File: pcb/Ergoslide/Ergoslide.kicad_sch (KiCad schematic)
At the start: 170 parts

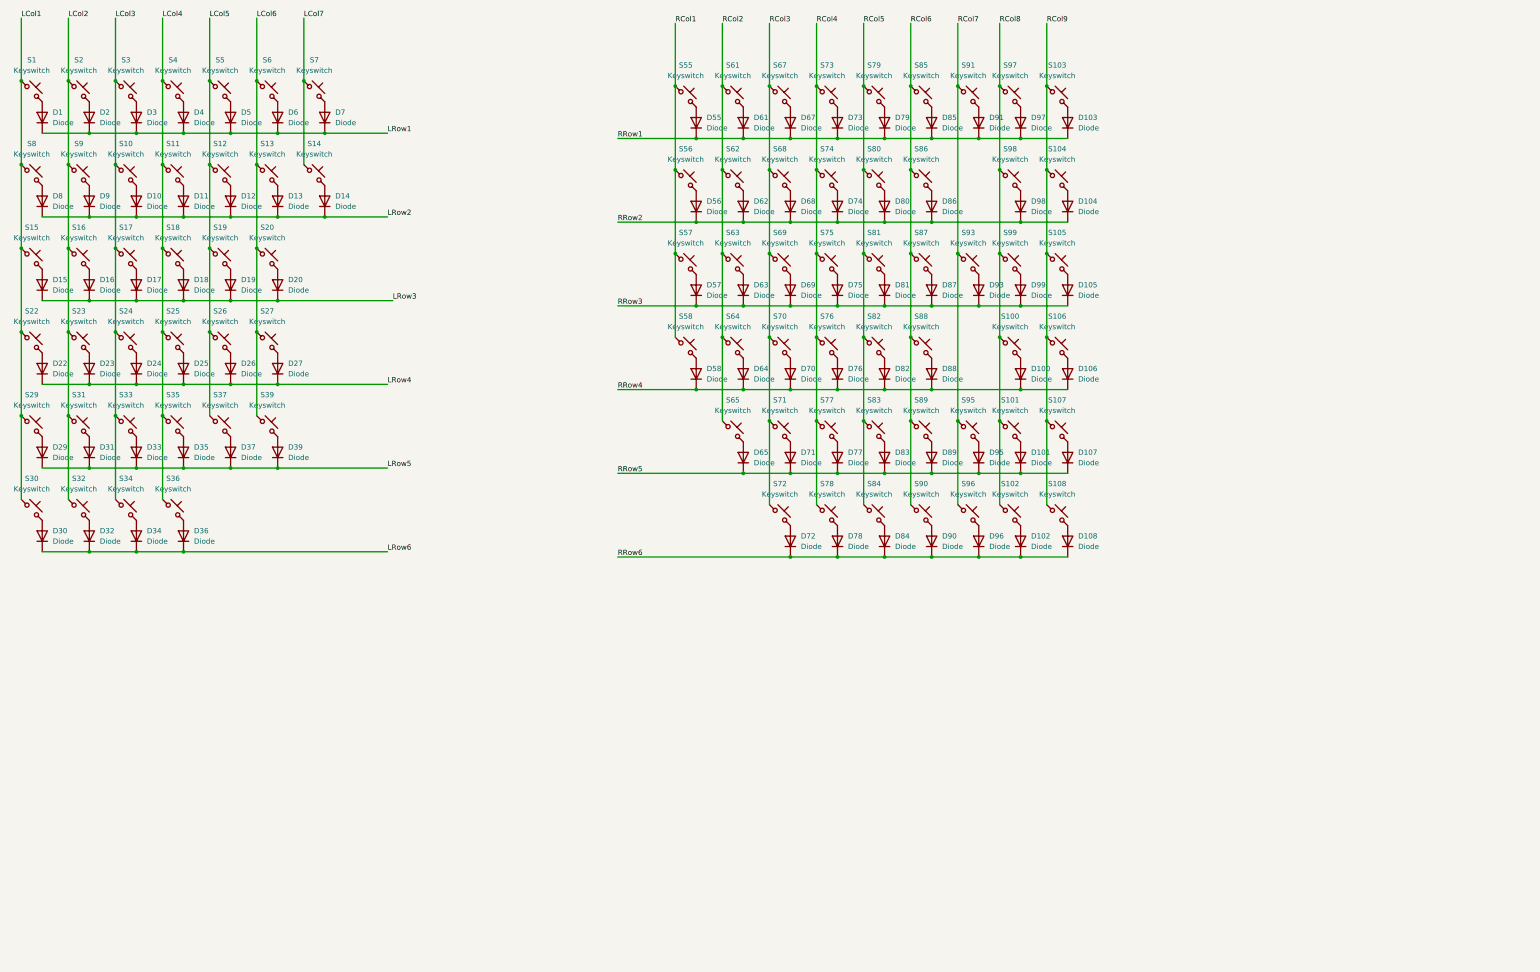
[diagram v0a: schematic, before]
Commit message: Start wiring up the PCB
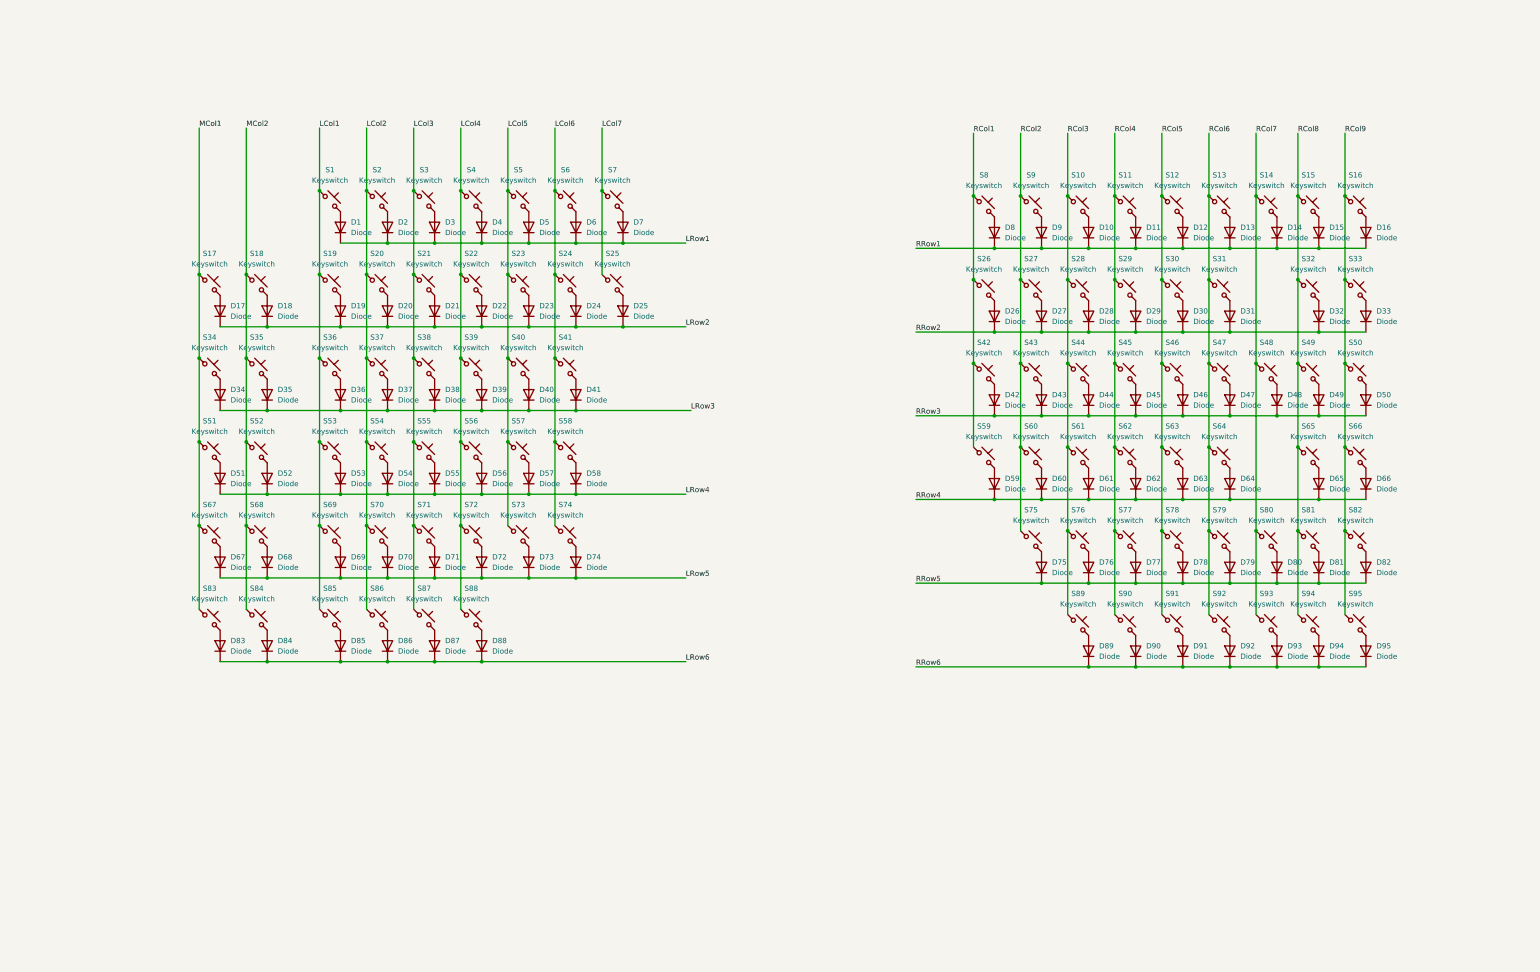
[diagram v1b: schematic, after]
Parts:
- added D17, D18, D34, D35, D51, D52, D67, D68, D83, D84: Diode, ScottoKeebs_Components:Diode_SOD-123, symbol ScottoKeebs:Placeholder_Diode
- added S17, S18, S34, S35, S51, S52, S67, S68, S83, S84: Keyswitch, Gateron_KS33_Hotswap:Gateron-KS33-Hotswap-1U, symbol ScottoKeebs:Placeholder_Keyswitch
- D1, D2, D3, D4, D5, D6, D7, D77: footprint (none) -> ScottoKeebs_Components:Diode_SOD-123
- D10: renamed from D67; footprint (none) -> ScottoKeebs_Components:Diode_SOD-123
- D11: renamed from D73; footprint (none) -> ScottoKeebs_Components:Diode_SOD-123
- D12: renamed from D79; footprint (none) -> ScottoKeebs_Components:Diode_SOD-123
- D13: renamed from D85; footprint (none) -> ScottoKeebs_Components:Diode_SOD-123
- D14: renamed from D91; footprint (none) -> ScottoKeebs_Components:Diode_SOD-123
- D15: renamed from D97; footprint (none) -> ScottoKeebs_Components:Diode_SOD-123
- D16: renamed from D103; footprint (none) -> ScottoKeebs_Components:Diode_SOD-123
- D19: renamed from D8; footprint (none) -> ScottoKeebs_Components:Diode_SOD-123
- D20: renamed from D9; footprint (none) -> ScottoKeebs_Components:Diode_SOD-123
- D21: renamed from D10; footprint (none) -> ScottoKeebs_Components:Diode_SOD-123
- D22: renamed from D11; footprint (none) -> ScottoKeebs_Components:Diode_SOD-123
- D23: renamed from D12; footprint (none) -> ScottoKeebs_Components:Diode_SOD-123
- D24: renamed from D13; footprint (none) -> ScottoKeebs_Components:Diode_SOD-123
- D25: renamed from D14; footprint (none) -> ScottoKeebs_Components:Diode_SOD-123
- D26: renamed from D56; footprint (none) -> ScottoKeebs_Components:Diode_SOD-123
- D27: renamed from D62; footprint (none) -> ScottoKeebs_Components:Diode_SOD-123
- D28: renamed from D68; footprint (none) -> ScottoKeebs_Components:Diode_SOD-123
- D29: renamed from D74; footprint (none) -> ScottoKeebs_Components:Diode_SOD-123
- D30: renamed from D80; footprint (none) -> ScottoKeebs_Components:Diode_SOD-123
- D31: renamed from D86; footprint (none) -> ScottoKeebs_Components:Diode_SOD-123
- D32: renamed from D98; footprint (none) -> ScottoKeebs_Components:Diode_SOD-123
- D33: renamed from D104; footprint (none) -> ScottoKeebs_Components:Diode_SOD-123
- D36: renamed from D15; footprint (none) -> ScottoKeebs_Components:Diode_SOD-123
- D37: renamed from D16; footprint (none) -> ScottoKeebs_Components:Diode_SOD-123
- D38: renamed from D17; footprint (none) -> ScottoKeebs_Components:Diode_SOD-123
- D39: renamed from D18; footprint (none) -> ScottoKeebs_Components:Diode_SOD-123
- D40: renamed from D19; footprint (none) -> ScottoKeebs_Components:Diode_SOD-123
- D41: renamed from D20; footprint (none) -> ScottoKeebs_Components:Diode_SOD-123
- D42: renamed from D57; footprint (none) -> ScottoKeebs_Components:Diode_SOD-123
- D43: renamed from D63; footprint (none) -> ScottoKeebs_Components:Diode_SOD-123
- D44: renamed from D69; footprint (none) -> ScottoKeebs_Components:Diode_SOD-123
- D45: renamed from D75; footprint (none) -> ScottoKeebs_Components:Diode_SOD-123
- D46: renamed from D81; footprint (none) -> ScottoKeebs_Components:Diode_SOD-123
- D47: renamed from D87; footprint (none) -> ScottoKeebs_Components:Diode_SOD-123
- D48: renamed from D93; footprint (none) -> ScottoKeebs_Components:Diode_SOD-123
- D49: renamed from D99; footprint (none) -> ScottoKeebs_Components:Diode_SOD-123
- D50: renamed from D105; footprint (none) -> ScottoKeebs_Components:Diode_SOD-123
- D53: renamed from D22; footprint (none) -> ScottoKeebs_Components:Diode_SOD-123
- D54: renamed from D23; footprint (none) -> ScottoKeebs_Components:Diode_SOD-123
- D55: renamed from D24; footprint (none) -> ScottoKeebs_Components:Diode_SOD-123
- D56: renamed from D25; footprint (none) -> ScottoKeebs_Components:Diode_SOD-123
- D57: renamed from D26; footprint (none) -> ScottoKeebs_Components:Diode_SOD-123
- D58: renamed from D27; footprint (none) -> ScottoKeebs_Components:Diode_SOD-123
- D59: renamed from D58; footprint (none) -> ScottoKeebs_Components:Diode_SOD-123
- D60: renamed from D64; footprint (none) -> ScottoKeebs_Components:Diode_SOD-123
- D61: renamed from D70; footprint (none) -> ScottoKeebs_Components:Diode_SOD-123
- D62: renamed from D76; footprint (none) -> ScottoKeebs_Components:Diode_SOD-123
- D63: renamed from D82; footprint (none) -> ScottoKeebs_Components:Diode_SOD-123
- D64: renamed from D88; footprint (none) -> ScottoKeebs_Components:Diode_SOD-123
- D65: renamed from D100; footprint (none) -> ScottoKeebs_Components:Diode_SOD-123
- D66: renamed from D106; footprint (none) -> ScottoKeebs_Components:Diode_SOD-123
- D69: renamed from D29; footprint (none) -> ScottoKeebs_Components:Diode_SOD-123
- D70: renamed from D31; footprint (none) -> ScottoKeebs_Components:Diode_SOD-123
- D71: renamed from D33; footprint (none) -> ScottoKeebs_Components:Diode_SOD-123
- D72: renamed from D35; footprint (none) -> ScottoKeebs_Components:Diode_SOD-123
- D73: renamed from D37; footprint (none) -> ScottoKeebs_Components:Diode_SOD-123
- D74: renamed from D39; footprint (none) -> ScottoKeebs_Components:Diode_SOD-123
- D75: renamed from D65; footprint (none) -> ScottoKeebs_Components:Diode_SOD-123
- D76: renamed from D71; footprint (none) -> ScottoKeebs_Components:Diode_SOD-123
- D78: renamed from D83; footprint (none) -> ScottoKeebs_Components:Diode_SOD-123
- D79: renamed from D89; footprint (none) -> ScottoKeebs_Components:Diode_SOD-123
- D8: renamed from D55; footprint (none) -> ScottoKeebs_Components:Diode_SOD-123
- D80: renamed from D95; footprint (none) -> ScottoKeebs_Components:Diode_SOD-123
- D81: renamed from D101; footprint (none) -> ScottoKeebs_Components:Diode_SOD-123
- D82: renamed from D107; footprint (none) -> ScottoKeebs_Components:Diode_SOD-123
- D85: renamed from D30; footprint (none) -> ScottoKeebs_Components:Diode_SOD-123
- D86: renamed from D32; footprint (none) -> ScottoKeebs_Components:Diode_SOD-123
- D87: renamed from D34; footprint (none) -> ScottoKeebs_Components:Diode_SOD-123
- D88: renamed from D36; footprint (none) -> ScottoKeebs_Components:Diode_SOD-123
- D89: renamed from D72; footprint (none) -> ScottoKeebs_Components:Diode_SOD-123
- D9: renamed from D61; footprint (none) -> ScottoKeebs_Components:Diode_SOD-123
- D90: renamed from D78; footprint (none) -> ScottoKeebs_Components:Diode_SOD-123
- D91: renamed from D84; footprint (none) -> ScottoKeebs_Components:Diode_SOD-123
- D92: renamed from D90; footprint (none) -> ScottoKeebs_Components:Diode_SOD-123
- D93: renamed from D96; footprint (none) -> ScottoKeebs_Components:Diode_SOD-123
- D94: renamed from D102; footprint (none) -> ScottoKeebs_Components:Diode_SOD-123
- D95: renamed from D108; footprint (none) -> ScottoKeebs_Components:Diode_SOD-123
- S1, S2, S3, S4, S5, S6, S7, S77: footprint (none) -> Gateron_KS33_Hotswap:Gateron-KS33-Hotswap-1U
- S10: renamed from S67; footprint (none) -> Gateron_KS33_Hotswap:Gateron-KS33-Hotswap-1U
- S11: renamed from S73; footprint (none) -> Gateron_KS33_Hotswap:Gateron-KS33-Hotswap-1U
- S12: renamed from S79; footprint (none) -> Gateron_KS33_Hotswap:Gateron-KS33-Hotswap-1U
- S13: renamed from S85; footprint (none) -> Gateron_KS33_Hotswap:Gateron-KS33-Hotswap-1U
- S14: renamed from S91; footprint (none) -> Gateron_KS33_Hotswap:Gateron-KS33-Hotswap-1U
- S15: renamed from S97; footprint (none) -> Gateron_KS33_Hotswap:Gateron-KS33-Hotswap-1U
- S16: renamed from S103; footprint (none) -> Gateron_KS33_Hotswap:Gateron-KS33-Hotswap-1U
- S19: renamed from S8; footprint (none) -> Gateron_KS33_Hotswap:Gateron-KS33-Hotswap-1U
- S20: renamed from S9; footprint (none) -> Gateron_KS33_Hotswap:Gateron-KS33-Hotswap-1U
- S21: renamed from S10; footprint (none) -> Gateron_KS33_Hotswap:Gateron-KS33-Hotswap-1U
- S22: renamed from S11; footprint (none) -> Gateron_KS33_Hotswap:Gateron-KS33-Hotswap-1U
- S23: renamed from S12; footprint (none) -> Gateron_KS33_Hotswap:Gateron-KS33-Hotswap-1U
- S24: renamed from S13; footprint (none) -> Gateron_KS33_Hotswap:Gateron-KS33-Hotswap-1U
- S25: renamed from S14; footprint (none) -> Gateron_KS33_Hotswap:Gateron-KS33-Hotswap-1U
- S26: renamed from S56; footprint (none) -> Gateron_KS33_Hotswap:Gateron-KS33-Hotswap-1U
- S27: renamed from S62; footprint (none) -> Gateron_KS33_Hotswap:Gateron-KS33-Hotswap-1U
- S28: renamed from S68; footprint (none) -> Gateron_KS33_Hotswap:Gateron-KS33-Hotswap-1U
- S29: renamed from S74; footprint (none) -> Gateron_KS33_Hotswap:Gateron-KS33-Hotswap-1U
- S30: renamed from S80; footprint (none) -> Gateron_KS33_Hotswap:Gateron-KS33-Hotswap-1U
- S31: renamed from S86; footprint (none) -> Gateron_KS33_Hotswap:Gateron-KS33-Hotswap-1U
- S32: renamed from S98; footprint (none) -> Gateron_KS33_Hotswap:Gateron-KS33-Hotswap-2U
- S33: renamed from S104; footprint (none) -> Gateron_KS33_Hotswap:Gateron-KS33-Hotswap-1U
- S36: renamed from S15; footprint (none) -> Gateron_KS33_Hotswap:Gateron-KS33-Hotswap-1.5U
- S37: renamed from S16; footprint (none) -> Gateron_KS33_Hotswap:Gateron-KS33-Hotswap-1U
- S38: renamed from S17; footprint (none) -> Gateron_KS33_Hotswap:Gateron-KS33-Hotswap-1U
- S39: renamed from S18; footprint (none) -> Gateron_KS33_Hotswap:Gateron-KS33-Hotswap-1U
- S40: renamed from S19; footprint (none) -> Gateron_KS33_Hotswap:Gateron-KS33-Hotswap-1U
- S41: renamed from S20; footprint (none) -> Gateron_KS33_Hotswap:Gateron-KS33-Hotswap-1U
- S42: renamed from S57; footprint (none) -> Gateron_KS33_Hotswap:Gateron-KS33-Hotswap-1U
- S43: renamed from S63; footprint (none) -> Gateron_KS33_Hotswap:Gateron-KS33-Hotswap-1U
- S44: renamed from S69; footprint (none) -> Gateron_KS33_Hotswap:Gateron-KS33-Hotswap-1U
- S45: renamed from S75; footprint (none) -> Gateron_KS33_Hotswap:Gateron-KS33-Hotswap-1U
- S46: renamed from S81; footprint (none) -> Gateron_KS33_Hotswap:Gateron-KS33-Hotswap-1U
- S47: renamed from S87; footprint (none) -> Gateron_KS33_Hotswap:Gateron-KS33-Hotswap-1U
- S48: renamed from S93; footprint (none) -> Gateron_KS33_Hotswap:Gateron-KS33-Hotswap-1U
- S49: renamed from S99; footprint (none) -> Gateron_KS33_Hotswap:Gateron-KS33-Hotswap-1.5U
- S50: renamed from S105; footprint (none) -> Gateron_KS33_Hotswap:Gateron-KS33-Hotswap-1U
- S53: renamed from S22; footprint (none) -> Gateron_KS33_Hotswap:Gateron-KS33-Hotswap-1.75U
- S54: renamed from S23; footprint (none) -> Gateron_KS33_Hotswap:Gateron-KS33-Hotswap-1U
- S55: renamed from S24; footprint (none) -> Gateron_KS33_Hotswap:Gateron-KS33-Hotswap-1U
- S56: renamed from S25; footprint (none) -> Gateron_KS33_Hotswap:Gateron-KS33-Hotswap-1U
- S57: renamed from S26; footprint (none) -> Gateron_KS33_Hotswap:Gateron-KS33-Hotswap-1U
- S58: renamed from S27; footprint (none) -> Gateron_KS33_Hotswap:Gateron-KS33-Hotswap-1U
- S59: renamed from S58; footprint (none) -> Gateron_KS33_Hotswap:Gateron-KS33-Hotswap-1U
- S60: renamed from S64; footprint (none) -> Gateron_KS33_Hotswap:Gateron-KS33-Hotswap-1U
- S61: renamed from S70; footprint (none) -> Gateron_KS33_Hotswap:Gateron-KS33-Hotswap-1U
- S62: renamed from S76; footprint (none) -> Gateron_KS33_Hotswap:Gateron-KS33-Hotswap-1U
- S63: renamed from S82; footprint (none) -> Gateron_KS33_Hotswap:Gateron-KS33-Hotswap-1U
- S64: renamed from S88; footprint (none) -> Gateron_KS33_Hotswap:Gateron-KS33-Hotswap-1U
- S65: renamed from S100; footprint (none) -> Gateron_KS33_Hotswap:Gateron-KS33-Hotswap-2.25U
- S66: renamed from S106; footprint (none) -> Gateron_KS33_Hotswap:Gateron-KS33-Hotswap-1U
- S69: renamed from S29; footprint (none) -> Gateron_KS33_Hotswap:Gateron-KS33-Hotswap-2.25U
- S70: renamed from S31; footprint (none) -> Gateron_KS33_Hotswap:Gateron-KS33-Hotswap-1U
- S71: renamed from S33; footprint (none) -> Gateron_KS33_Hotswap:Gateron-KS33-Hotswap-1U
- S72: renamed from S35; footprint (none) -> Gateron_KS33_Hotswap:Gateron-KS33-Hotswap-1U
- S73: renamed from S37; footprint (none) -> Gateron_KS33_Hotswap:Gateron-KS33-Hotswap-1U
- S74: renamed from S39; footprint (none) -> Gateron_KS33_Hotswap:Gateron-KS33-Hotswap-1U
- S75: renamed from S65; footprint (none) -> Gateron_KS33_Hotswap:Gateron-KS33-Hotswap-1U
- S76: renamed from S71; footprint (none) -> Gateron_KS33_Hotswap:Gateron-KS33-Hotswap-1U
- S78: renamed from S83; footprint (none) -> Gateron_KS33_Hotswap:Gateron-KS33-Hotswap-1U
- S79: renamed from S89; footprint (none) -> Gateron_KS33_Hotswap:Gateron-KS33-Hotswap-1U
- S8: renamed from S55; footprint (none) -> Gateron_KS33_Hotswap:Gateron-KS33-Hotswap-1U
- S80: renamed from S95; footprint (none) -> Gateron_KS33_Hotswap:Gateron-KS33-Hotswap-1.75U
- S81: renamed from S101; footprint (none) -> Gateron_KS33_Hotswap:Gateron-KS33-Hotswap-1U
- S82: renamed from S107; footprint (none) -> Gateron_KS33_Hotswap:Gateron-KS33-Hotswap-1U
- S85: renamed from S30; footprint (none) -> Gateron_KS33_Hotswap:Gateron-KS33-Hotswap-1.25U
- S86: renamed from S32; footprint (none) -> Gateron_KS33_Hotswap:Gateron-KS33-Hotswap-1.25U
- S87: renamed from S34; footprint (none) -> Gateron_KS33_Hotswap:Gateron-KS33-Hotswap-1.25U
- S88: renamed from S36; footprint (none) -> Gateron_KS33_Hotswap:Gateron-KS33-Hotswap-2.75U
- S89: renamed from S72; footprint (none) -> Gateron_KS33_Hotswap:Gateron-KS33-Hotswap-2.25U
- S9: renamed from S61; footprint (none) -> Gateron_KS33_Hotswap:Gateron-KS33-Hotswap-1U
- S90: renamed from S78; footprint (none) -> Gateron_KS33_Hotswap:Gateron-KS33-Hotswap-1.25U
- S91: renamed from S84; footprint (none) -> Gateron_KS33_Hotswap:Gateron-KS33-Hotswap-1U
- S92: renamed from S90; footprint (none) -> Gateron_KS33_Hotswap:Gateron-KS33-Hotswap-1.25U
- S93: renamed from S96; footprint (none) -> Gateron_KS33_Hotswap:Gateron-KS33-Hotswap-1U
- S94: renamed from S102; footprint (none) -> Gateron_KS33_Hotswap:Gateron-KS33-Hotswap-1U
- S95: renamed from S108; footprint (none) -> Gateron_KS33_Hotswap:Gateron-KS33-Hotswap-1U
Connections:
- net LRow2: now also D17.1 (K), D18.1 (K)
- net LRow3: now also D34.1 (K), D35.1 (K)
- net LRow4: now also D51.1 (K), D52.1 (K)
- net LRow5: now also D67.1 (K), D68.1 (K)
- net LRow6: now also D83.1 (K), D84.1 (K)
- new net: D34.2 (A), S34.2
- new net: D51.2 (A), S51.2
- new net: D67.2 (A), S67.2
- new net: D83.2 (A), S83.2
- new net: D52.2 (A), S52.2
- new net: D18.2 (A), S18.2
- new net: D84.2 (A), S84.2
- new net: D35.2 (A), S35.2
- new net: D17.2 (A), S17.2
- new net: D68.2 (A), S68.2
- new net MCol1: S17.1, S34.1, S51.1, S67.1, S83.1
- new net MCol2: S18.1, S35.1, S52.1, S68.1, S84.1
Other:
- moved on the sheet: D1, D10, D11, D12, D13, D14, D15, D16, D19, D2, D20, D21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

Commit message: Muck about with custom footprints and symbols for the Supermini
Started wiring the Supermini in to the left side matrix
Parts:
- added J1, J2: Conn_01x02_Socket, Connector_JST:JST_PH_S2B-PH-K_1x02_P2.00mm_Horizontal, symbol Connector:Conn_01x02_Socket
- added LeftController1, RightController1: ~, supermini-nrf52840-kicad:SuperMini NRF52840, symbol custom-symbols:SuperMini_nRF52840
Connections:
- net LCol1: now also LeftController1.11 (D8_P1.04)
- net LCol2: now also LeftController1.10 (D7_P0.11)
- net LCol3: now also LeftController1.9 (D6_P1.00)
- net LCol4: now also LeftController1.8 (D5_P0.24)
- net LCol5: now also LeftController1.7 (D4_P0.22)
- net LCol6: now also LeftController1.6 (D3_P0.20)
- net LCol7: now also LeftController1.5 (D2_P0.17)
- net LRow1: now also LeftController1.19 (D19_P0.02)
- net LRow2: now also LeftController1.20 (D18_P1.15)
- net LRow3: now also LeftController1.21 (D15_P1.13)
- net LRow4: now also LeftController1.22 (D14_P1.11)
- net LRow5: now also LeftController1.23 (D16_P0.10)
- net LRow6: now also LeftController1.24 (D10_P0.09)
- net MCol1: now also LeftController1.17 (D21_P0.31)
- net MCol2: now also LeftController1.18 (D20_P0.29)
- new net: J2.1 (Pin_1), LeftController1.28 (B-)
- new net: J2.2 (Pin_2), LeftController1.29 (B+)

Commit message: Clean up pcb directory in Git
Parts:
- added H1, H2, H3, H4: MountingHole, MountingHole:MountingHole_2.2mm_M2, symbol Mechanical:MountingHole
- added SW1: Switch, Button_Switch_SMD:Panasonic_EVQPUL_EVQPUC, symbol ScottoKeebs:Placeholder_Switch
- added SW2: Power Switch, ScottoKeebs_Components:Switch_SSAL220100, symbol Switch:SW_SPST
- added TP1: B- testpoint, TestPoint:TestPoint_Pad_2.0x2.0mm, symbol Connector:TestPoint
- added TP2: B+ testpoint, TestPoint:TestPoint_Pad_2.0x2.0mm, symbol Connector:TestPoint
- added TP3: GND testpoint, TestPoint:TestPoint_Pad_2.0x2.0mm, symbol Connector:TestPoint
- added TP4: RST testpoint, TestPoint:TestPoint_Pad_2.0x2.0mm, symbol Connector:TestPoint
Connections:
- net at LeftController1.28 (B-): now also SW2.1 (A); no longer J2.1 (Pin_1)
- net at J2.2 (Pin_2), LeftController1.29 (B+): now also TP2.1
- net at LeftController1.14 (GND): now also SW1.1, TP3.1
- net at LeftController1.15 (RST): now also SW1.2, TP4.1
- new net: J2.1 (Pin_1), SW2.2 (B), TP1.1

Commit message: Add the bottom pattern image for the case, as well as the Fusion project and exported STEP file
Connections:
- net at J1.1 (Pin_1): now also RightController1.1 (B-)
- net at J1.2 (Pin_2): now also RightController1.26 (B+)
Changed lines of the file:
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@@
+	(wire
+		(pts
+			(xy 256.54 205.74) (xy 256.54 189.23)
+		)
+		(stroke
+			(width 0)
+			(type default)
+		)
+	)
 	(wire
 		(pts
@@
 	(wire
 		(pts
+			(xy 256.54 189.23) (xy 323.85 189.23)
+		)
+		(stroke
+			(width 0)
+			(type default)
+		)
+	)
+	(wire
+		(pts
 			(xy 149.86 130.81) (xy 149.86 151.13)
 		)
@@
 	(wire
 		(pts
+			(xy 260.35 203.2) (xy 260.35 194.31)
+		)
+		(stroke
+			(width 0)
+			(type default)
+		)
+	)
+	(wire
+		(pts
 			(xy 308.61 132.08) (xy 308.61 152.4)
 		)
@@
 	(wire
 		(pts
+			(xy 323.85 189.23) (xy 323.85 194.31)
+		)
+		(stroke
+			(width 0)
+			(type default)
+		)
+	)
+	(wire
+		(pts
 			(xy 330.2 152.4) (xy 330.2 172.72)
 		)
@@
 	(wire
 		(pts
+			(xy 260.35 205.74) (xy 256.54 205.74)
+		)
+		(stroke
+			(width 0)
+			(type default)
+		)
+	)
+	(wire
+		(pts
 			(xy 256.54 104.14) (xy 267.97 104.14)
 		)
@@
 		)
 		(stroke
+			(width 0)
+			(type default)
+		)
+	)
+	(wire
+		(pts
+			(xy 260.35 194.31) (xy 290.83 194.31)
+		)
+		(stroke

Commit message: Add TL3330AF260GQ to the PCB, start wiring up the second half
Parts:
- removed TP1: B- testpoint, TestPoint:TestPoint_Pad_2.0x2.0mm, symbol Connector:TestPoint
- removed TP2: B+ testpoint, TestPoint:TestPoint_Pad_2.0x2.0mm, symbol Connector:TestPoint
- added BTN2, BTN4: Soft Off button, TL3330AF260QG:SW_TL3330AF260QG, symbol ScottoKeebs:Placeholder_Switch
- added BTN3: Reset button, TL3330AF260QG:SW_TL3330AF260QG, symbol ScottoKeebs:Placeholder_Switch
- added GND2: GND2 test point, TestPoint:TestPoint_Pad_2.0x2.0mm, symbol Connector:TestPoint
- added GND3: GND testpoint, TestPoint:TestPoint_Pad_2.0x2.0mm, symbol Connector:TestPoint
- added H10, H11, H12, H13, H14, H15, H16, H5, H6, H7, H8, H9: MountingHole, MountingHole:MountingHole_2.2mm_M2, symbol Mechanical:MountingHole
- added RST1, RST2: RST testpoint, TestPoint:TestPoint_Pad_2.0x2.0mm, symbol Connector:TestPoint
- added SOFF2: Soft-Off test point, TestPoint:TestPoint_Pad_2.0x2.0mm, symbol Connector:TestPoint
- BTN1: renamed from SW1; value Switch -> Reset button; footprint Button_Switch_SMD:Panasonic_EVQPUL_EVQPUC -> TL3330AF260QG:SW_TL3330AF260QG
- RightController1: footprint supermini-nrf52840-kicad:SuperMini NRF52840 -> supermini-nrf52840-kicad:SimpleMini NRF52840
- SOFF1: renamed from TP4; value RST testpoint -> Soft-Off test point
- SW1: renamed from SW2; footprint ScottoKeebs_Components:Switch_SSAL220100 -> Button_Switch_SMD:SW_SPDT_CK_JS102011SAQN
- renumbered TP3 to GND1, H4 to H1, H3 to H2, H1 to H3, H2 to H4, J2 to J1, J1 to J2
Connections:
- net LRow1: now also LeftController1.22 (D14_P1.11); no longer LeftController1.19 (D19_P0.02)
- net LRow2: now also LeftController1.21 (D15_P1.13); no longer LeftController1.20 (D18_P1.15)
- net LRow3: now also LeftController1.20 (D18_P1.15); no longer LeftController1.21 (D15_P1.13)
- net LRow4: now also LeftController1.19 (D19_P0.02); no longer LeftController1.22 (D14_P1.11)
- net LRow5: now also LeftController1.18 (D20_P0.29); no longer LeftController1.23 (D16_P0.10)
- net LRow6: now also LeftController1.17 (D21_P0.31); no longer LeftController1.24 (D10_P0.09)
- net MCol1: now also LeftController1.23 (D16_P0.10); no longer LeftController1.17 (D21_P0.31)
- net MCol2: now also LeftController1.24 (D10_P0.09); no longer LeftController1.18 (D20_P0.29)
- net RCol1: now also RightController1.5 (D2_P0.17)
- net RCol2: now also RightController1.6 (D3_P0.20)
- net RCol3: now also RightController1.7 (D4_P0.22)
- net RCol4: now also RightController1.8 (D5_P0.24)
- net RCol5: now also RightController1.9 (D6_P1.00)
- net RCol6: now also RightController1.10 (D7_P0.11)
- net RCol7: now also RightController1.11 (D8_P1.04)
- net RCol8: now also RightController1.12 (D9_P1.06)
- net RCol9: now also RightController1.24 (D10_P0.09)
- net RRow1: now also RightController1.18 (D20_P0.29)
- net RRow2: now also RightController1.19 (D19_P0.02)
- net RRow3: now also RightController1.20 (D18_P1.15)
- net RRow4: now also RightController1.21 (D15_P1.13)
- net RRow5: now also RightController1.22 (D14_P1.11)
- net RRow6: now also RightController1.23 (D16_P0.10)
- net at SW1.1 (A): now also J1.1 (Pin_1); no longer LeftController1.28 (B-)
- net at SW1.2 (B): now also LeftController1.28 (B-); no longer J1.1 (Pin_1)
- net at BTN1.2, LeftController1.15 (RST): now also RST1.1; no longer SOFF1.1
- net at RightController1.1 (D1_P0.06): no longer J2.1 (Pin_1)
- net at J2.2 (Pin_2): now also RightController1.29 (B+); no longer RightController1.26 (B+)
- net at RightController1.14 (GND): now also BTN3.1, BTN4.2, GND3.1
- net at RightController1.15 (RST): now also BTN3.2, RST2.1
- net at RightController1.17 (D21_P0.31): now also BTN4.1, SOFF2.1
- net at RightController1.28 (B-): now also J2.1 (Pin_1)
- net at LeftController1.12 (D9_P1.06): now also SOFF1.1, BTN2.1
- net at LeftController1.3 (GND): now also BTN2.2, GND2.1
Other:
- moved on the sheet: H1, H2, H3, H4, J2, SOFF1, SW1
